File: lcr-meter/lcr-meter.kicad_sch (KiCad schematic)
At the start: 0 parts

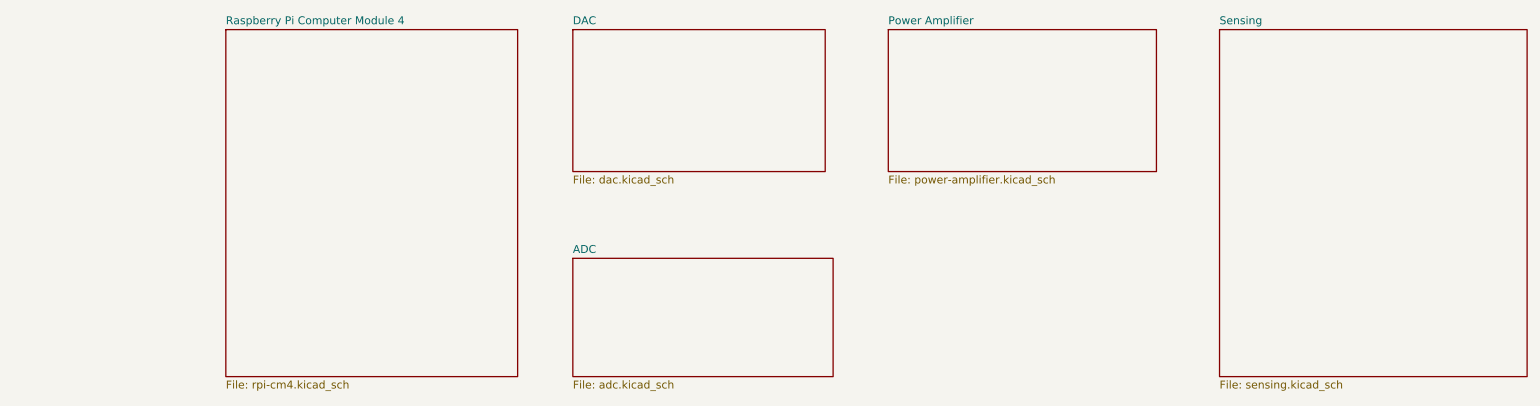
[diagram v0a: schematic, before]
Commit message: Added CM4, basics of functionality started
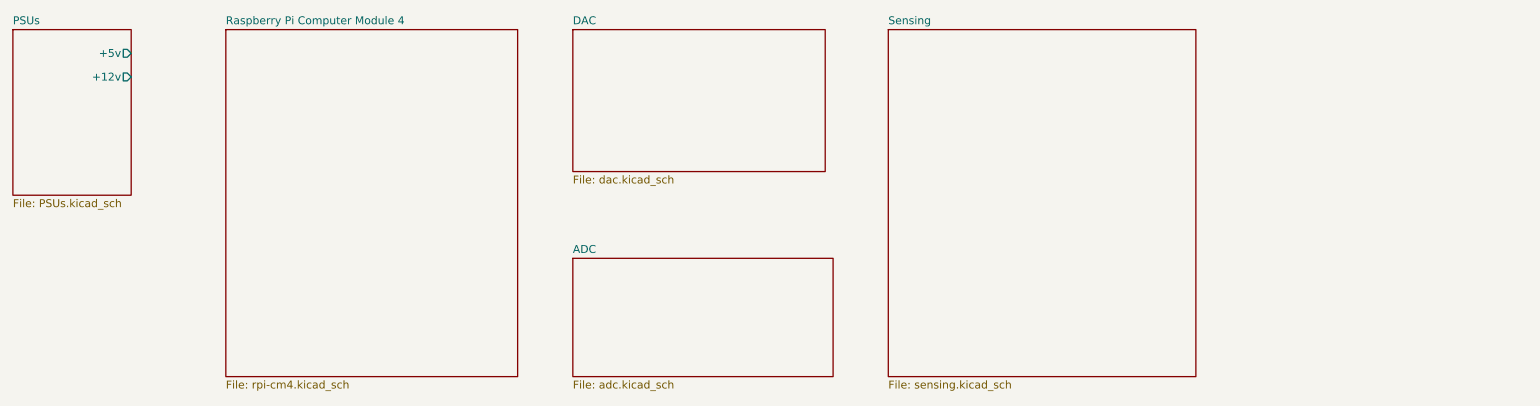
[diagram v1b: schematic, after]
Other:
- removed sheet Power Amplifier
- added sheet PSUs (PSUs.kicad_sch)
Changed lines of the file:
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@@
 	(sheet
 		(at 170.18 66.04)
-		(size 43.18 22.86)
-		(fields_autoplaced yes)
-		(stroke
-			(width 0.1524)
-			(type solid)
-		)
-		(fill
-			(color 0 0 0 0.0000)
-		)
-		(property "Sheetname" "Power Amplifier"
-			(at 170.18 65.3284 0)
-			(effects
-				(font
-					(size 1.27 1.27)
-				)
-				(justify left bottom)
-			)
-		)
-		(property "Sheetfile" "power-amplifier.kicad_sch"
-			(at 170.18 89.4846 0)
-			(effects
-				(font
-					(size 1.27 1.27)
-				)
-				(justify left top)
-			)
-		)
-		(instances
-			(project "lcr-meter"
-				(path "/ba333b18-b098-477b-9dd4-aab7b9764d9c"
-					(page "5")
-				)
-			)
-		)
-	)
-	(sheet
-		(at 223.52 66.04)
 		(size 49.53 55.88)
 		(fields_autoplaced yes)
@@
 		)
 		(property "Sheetname" "Sensing"
-			(at 223.52 65.3284 0)
+			(at 170.18 65.3284 0)
 			(effects
 				(font
@@
 		)
 		(property "Sheetfile" "sensing.kicad_sch"
-			(at 223.52 122.5046 0)
+			(at 170.18 122.5046 0)
 			(effects
 				(font
@@
 				)
 			)
+		)
+	)
+	(sheet
+		(at 29.21 66.04)
+		(size 19.05 26.67)
+		(fields_autoplaced yes)
+		(stroke
+			(width 0.1524)
+			(type solid)
+		)
+		(fill
+			(color 0 0 0 0.0000)
+		)
+		(property "Sheetname" "PSUs"
+			(at 29.21 65.3284 0)
+			(effects
+				(font
+					(size 1.27 1.27)
+				)
+				(justify left bottom)
+			)
+		)
+		(property "Sheetfile" "PSUs.kicad_sch"
+			(at 29.21 93.2946 0)
+			(effects
+				(font
+					(size 1.27 1.27)
+				)
+				(justify left top)
+			)
+		)
+		(property "Field2" ""
+			(at 29.21 66.04 0)
+			(effects
+				(font
+					(size 1.27 1.27)
+				)
+				(hide yes)
+			)
+		)
+		(pin "+5v" output
+			(at 48.26 69.85 0)
+			(effects
+				(font
+					(size 1.27 1.27)
+				)
+				(justify right)
+			)
+		)
+		(pin "+12v" output
+			(at 48.26 73.66 0)
+			(effects
+				(font
+					(size 1.27 1.27)
+				)
+				(justify right)
+			)
+		)
+		(instances
+			(project "lcr-meter"
+				(path "/ba333b18-b098-477b-9dd4-aab7b9764d9c"
+					(page "8")
+				)
+			)

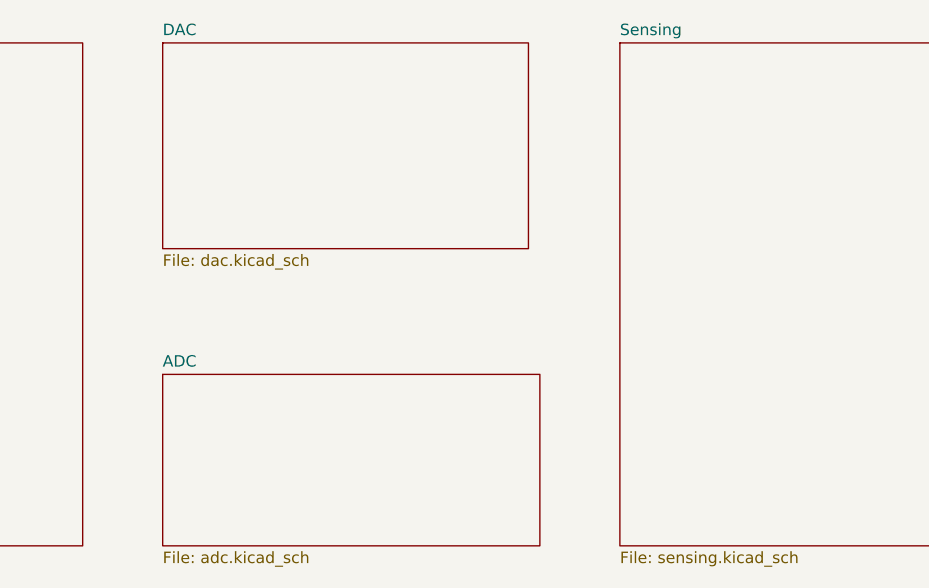
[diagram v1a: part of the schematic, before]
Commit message: Progress, removal of unnecessary components
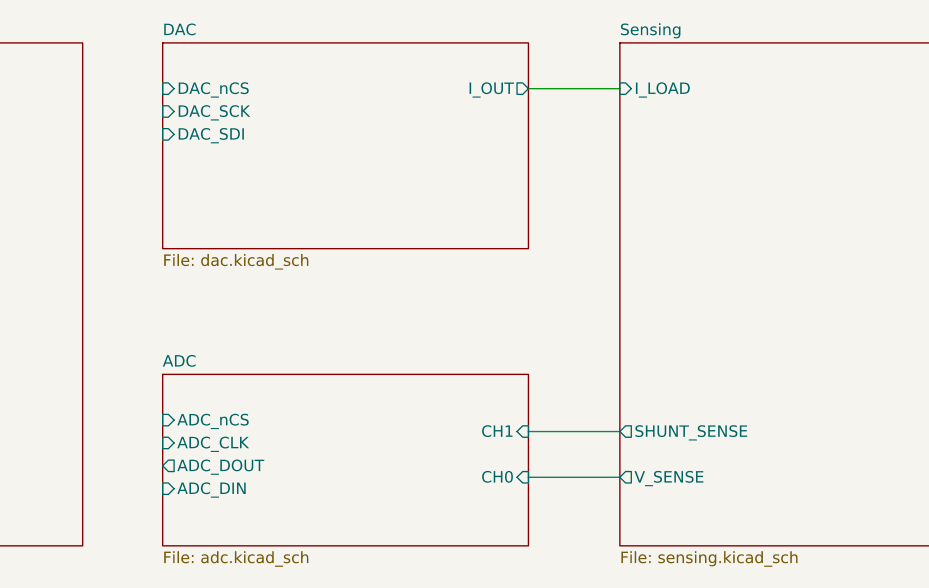
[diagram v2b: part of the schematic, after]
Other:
- sheet ADC ports: added ADC_CLK, ADC_DIN, ADC_DOUT, ADC_nCS, CH0, CH1; removed none
- sheet DAC ports: added DAC_SCK, DAC_SDI, DAC_nCS, I_OUT; removed none
- sheet Sensing ports: added I_LOAD, SHUNT_SENSE, V_SENSE; removed none
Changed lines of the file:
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@@
 	(generator_version "8.0")
 	(paper "A4")
+	(wire
+		(pts
+			(xy 160.02 71.12) (xy 170.18 71.12)
+		)
+		(stroke
+			(width 0)
+			(type default)
+		)
+	)
+	(wire
+		(pts
+			(xy 160.02 109.22) (xy 170.18 109.22)
+		)
+		(stroke
+			(width 0)
+			(type default)
+		)
+	)
+	(wire
+		(pts
+			(xy 160.02 114.3) (xy 170.18 114.3)
+		)
+		(stroke
+			(width 0)
+			(type default)
+		)
+	)
 	(sheet
 		(at 119.38 66.04)
@@
 			)
 		)
+		(pin "DAC_SCK" input
+			(at 119.38 73.66 180)
+			(effects
+				(font
+					(size 1.27 1.27)
+				)
+				(justify left)
+			)
+		)
+		(pin "DAC_SDI" input
+			(at 119.38 76.2 180)
+			(effects
+				(font
+					(size 1.27 1.27)
+				)
+				(justify left)
+			)
+		)
+		(pin "DAC_nCS" input
+			(at 119.38 71.12 180)
+			(effects
+				(font
+					(size 1.27 1.27)
+				)
+				(justify left)
+			)
+		)
+		(pin "I_OUT" output
+			(at 160.02 71.12 0)
+			(effects
+				(font
+					(size 1.27 1.27)
+				)
+				(justify right)
+			)
+		)
 		(instances
 			(project "lcr-meter"
@@
 			)
 		)
+		(pin "SHUNT_SENSE" output
+			(at 170.18 109.22 180)
+			(effects
+				(font
+					(size 1.27 1.27)
+				)
+				(justify left)
+			)
+		)
+		(pin "V_SENSE" output
+			(at 170.18 114.3 180)
+			(effects
+				(font
+					(size 1.27 1.27)
+				)
+				(justify left)
+			)
+		)
+		(pin "I_LOAD" input
+			(at 170.18 71.12 180)
+			(effects
+				(font
+					(size 1.27 1.27)
+				)
+				(justify left)
+			)
+		)
 		(instances
 			(project "lcr-meter"
@@
 	(sheet
 		(at 119.38 102.87)
-		(size 41.91 19.05)
+		(size 40.64 19.05)
 		(fields_autoplaced yes)
 		(stroke
@@
 			)
 		)
+		(pin "CH1" input
+			(at 160.02 109.22 0)
+			(effects
+				(font
+					(size 1.27 1.27)
+				)
+				(justify right)
+			)
+		)
+		(pin "CH0" input
+			(at 160.02 114.3 0)
+			(effects
+				(font
+					(size 1.27 1.27)
+				)
+				(justify right)
+			)
+		)
+		(pin "ADC_nCS" input
+			(at 119.38 107.95 180)
+			(effects
+				(font
+					(size 1.27 1.27)
+				)
+				(justify left)
+			)
+		)
+		(pin "ADC_CLK" input
+			(at 119.38 110.49 180)
+			(effects
+				(font
+					(size 1.27 1.27)
+				)
+				(justify left)
+			)
+		)
+		(pin "ADC_DOUT" output
+			(at 119.38 113.03 180)
+			(effects
+				(font
+					(size 1.27 1.27)
+				)
+				(justify left)
+			)
+		)
+		(pin "ADC_DIN" input
+			(at 119.38 115.57 180)
+			(effects
+				(font
+					(size 1.27 1.27)
+				)
+				(justify left)
+			)
+		)

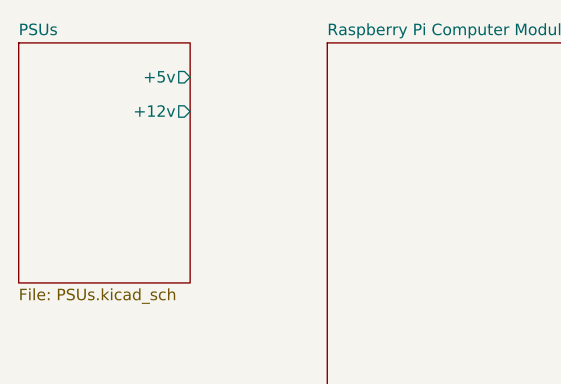
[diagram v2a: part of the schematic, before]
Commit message: Schematic updates, added -5V, finalized sensing
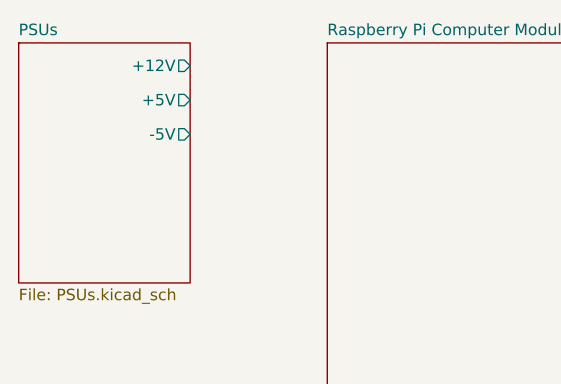
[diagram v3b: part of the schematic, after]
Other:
- sheet PSUs ports: added +12V, +5V, -5V; removed +12v, +5v
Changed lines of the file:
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@@
 			)
 		)
-		(pin "+5v" output
-			(at 48.26 69.85 0)
+		(pin "-5V" output
+			(at 48.26 76.2 0)
 			(effects
 				(font
@@
 			)
 		)
-		(pin "+12v" output
-			(at 48.26 73.66 0)
+		(pin "+12V" output
+			(at 48.26 68.58 0)
 			(effects
 				(font
+					(size 1.27 1.27)
+				)
+				(justify right)
+			)
+		)
+		(pin "+5V" output
+			(at 48.26 72.39 0)
+			(effects
+				(font

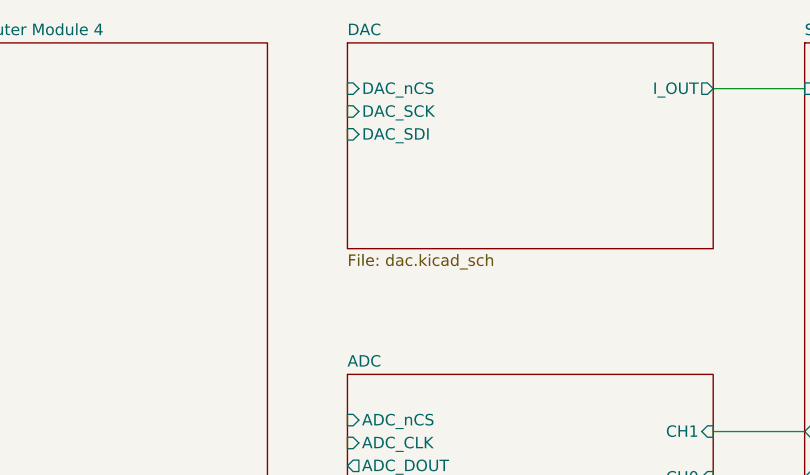
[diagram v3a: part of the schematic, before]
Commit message: Addressable LED test board
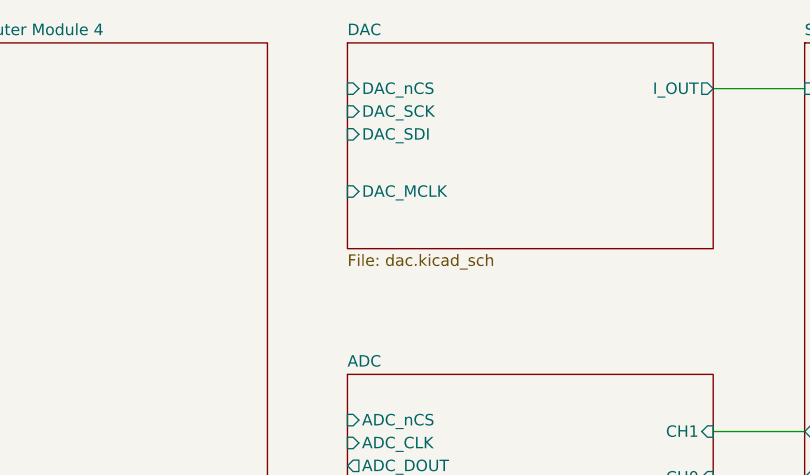
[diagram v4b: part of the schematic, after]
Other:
- sheet DAC ports: added DAC_MCLK; removed none
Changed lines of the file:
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@@
+			)
+		)
+		(pin "DAC_MCLK" input
+			(at 119.38 82.55 180)
+			(effects
+				(font
+					(size 1.27 1.27)
+				)
+				(justify left)
 			)
 		)

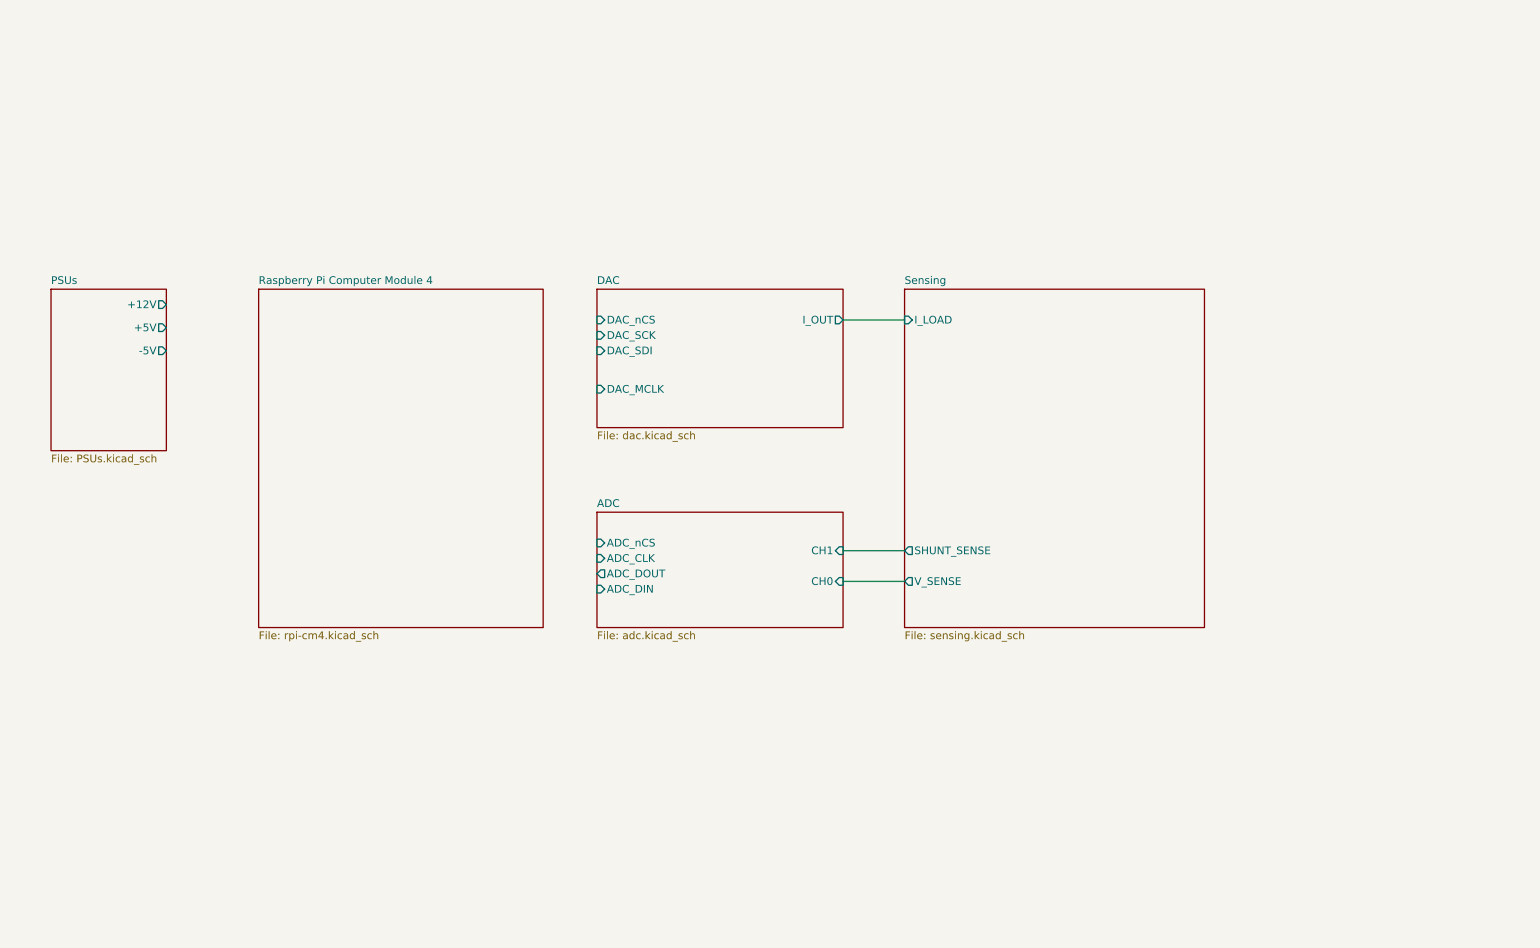
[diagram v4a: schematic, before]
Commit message: Schematic polishing, starting MCU schematic
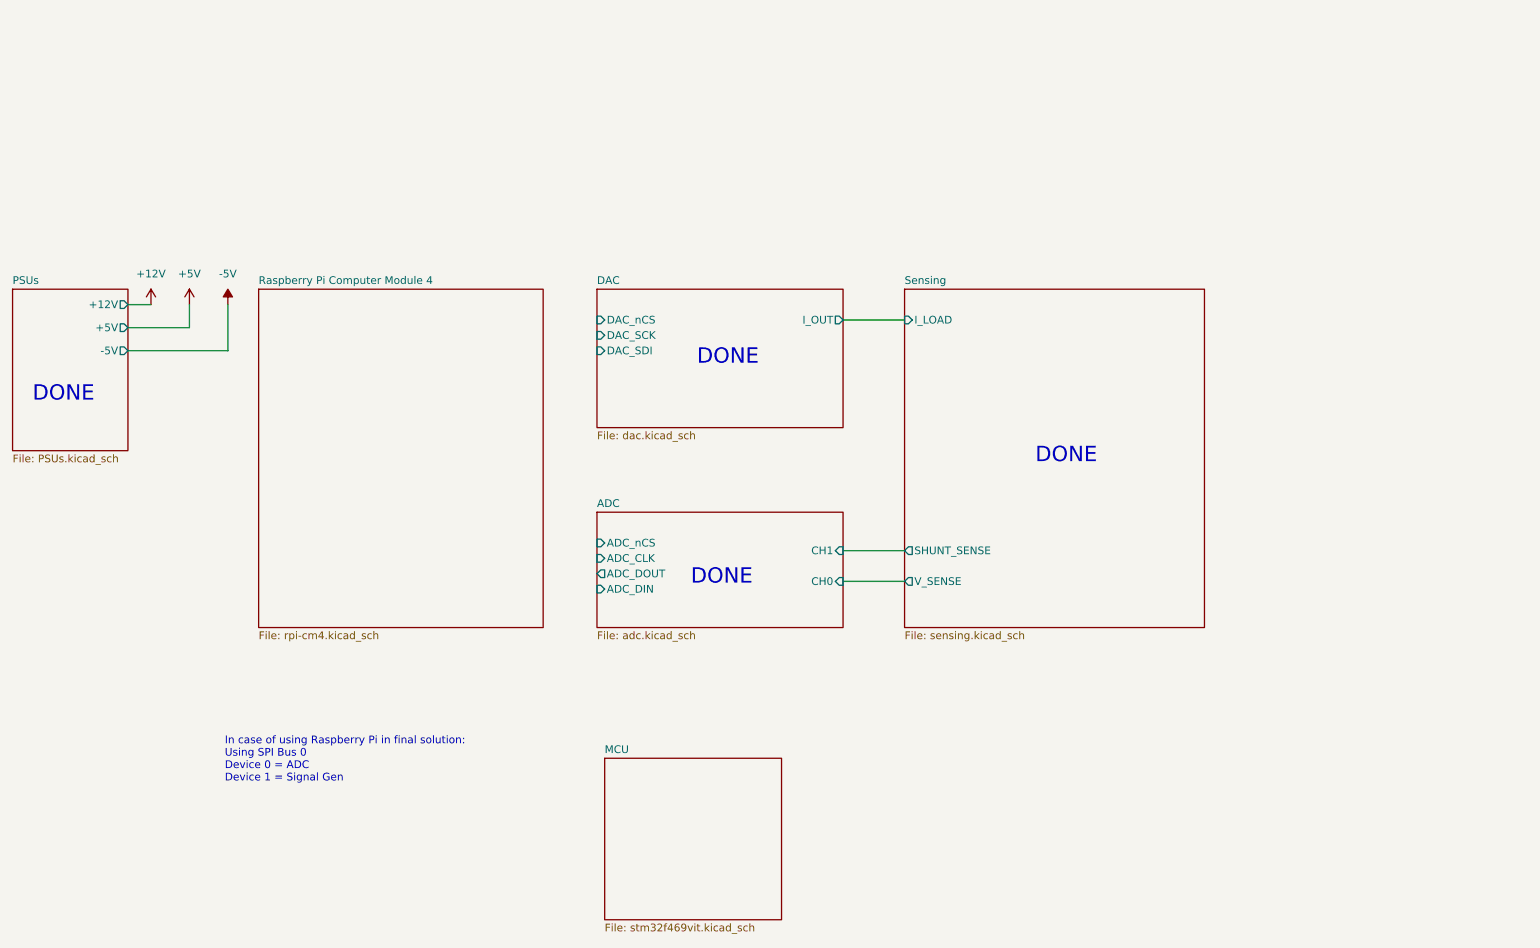
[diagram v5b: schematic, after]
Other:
- added sheet MCU (stm32f469vit.kicad_sch)
- sheet DAC ports: added none; removed DAC_MCLK
- note added: "DONE"
- note added: "In case of using Raspberry Pi in final solution: Using SPI Bus 0 Device 0 = ADC Device 1 = Signal Gen"

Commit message: Schematic completion
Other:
- removed sheet Raspberry Pi Computer Module 4
- added sheet LCD (lcd.kicad_sch)
- sheet MCU ports: added 3V3, AD9833_NCS, LCD_DC, LCD_LED, LCD_NCS, LCD_RST, MCP3202_NCS, SPI1_MISO, SPI1_MOSI, SPI1_SCK, SPI3_MISO, SPI3_MOSI, SPI3_SCK, STM32_ADC1_IN0, STM32_ADC2_IN1; removed none
- sheet PSUs ports: added +1V8, +3V3; removed none
- note removed: "In case of using Raspberry Pi in final solution: Using SPI Bus 0 Device 0 = ADC Device 1 = Signal Gen"
